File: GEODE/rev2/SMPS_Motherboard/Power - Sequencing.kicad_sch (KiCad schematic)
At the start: 0 parts

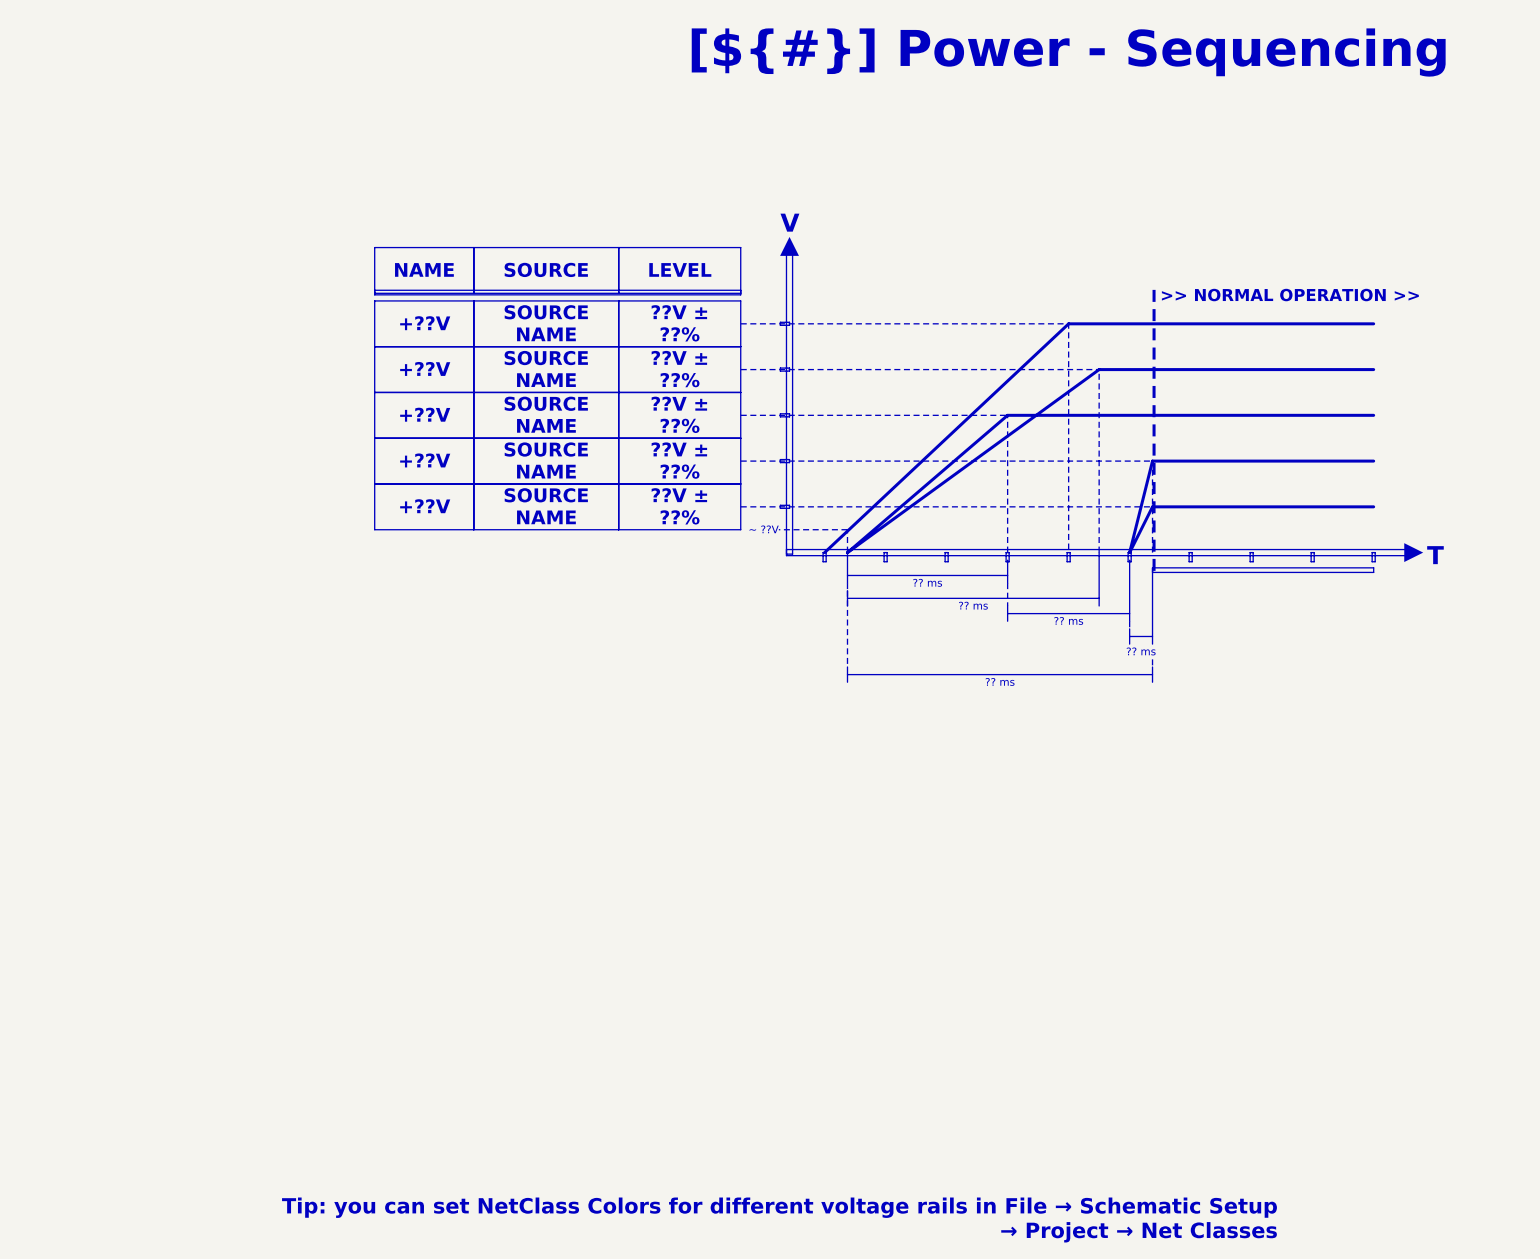
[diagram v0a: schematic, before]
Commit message: changed connectors, removed can, added fuse, disconnected EXTVCC in power generation
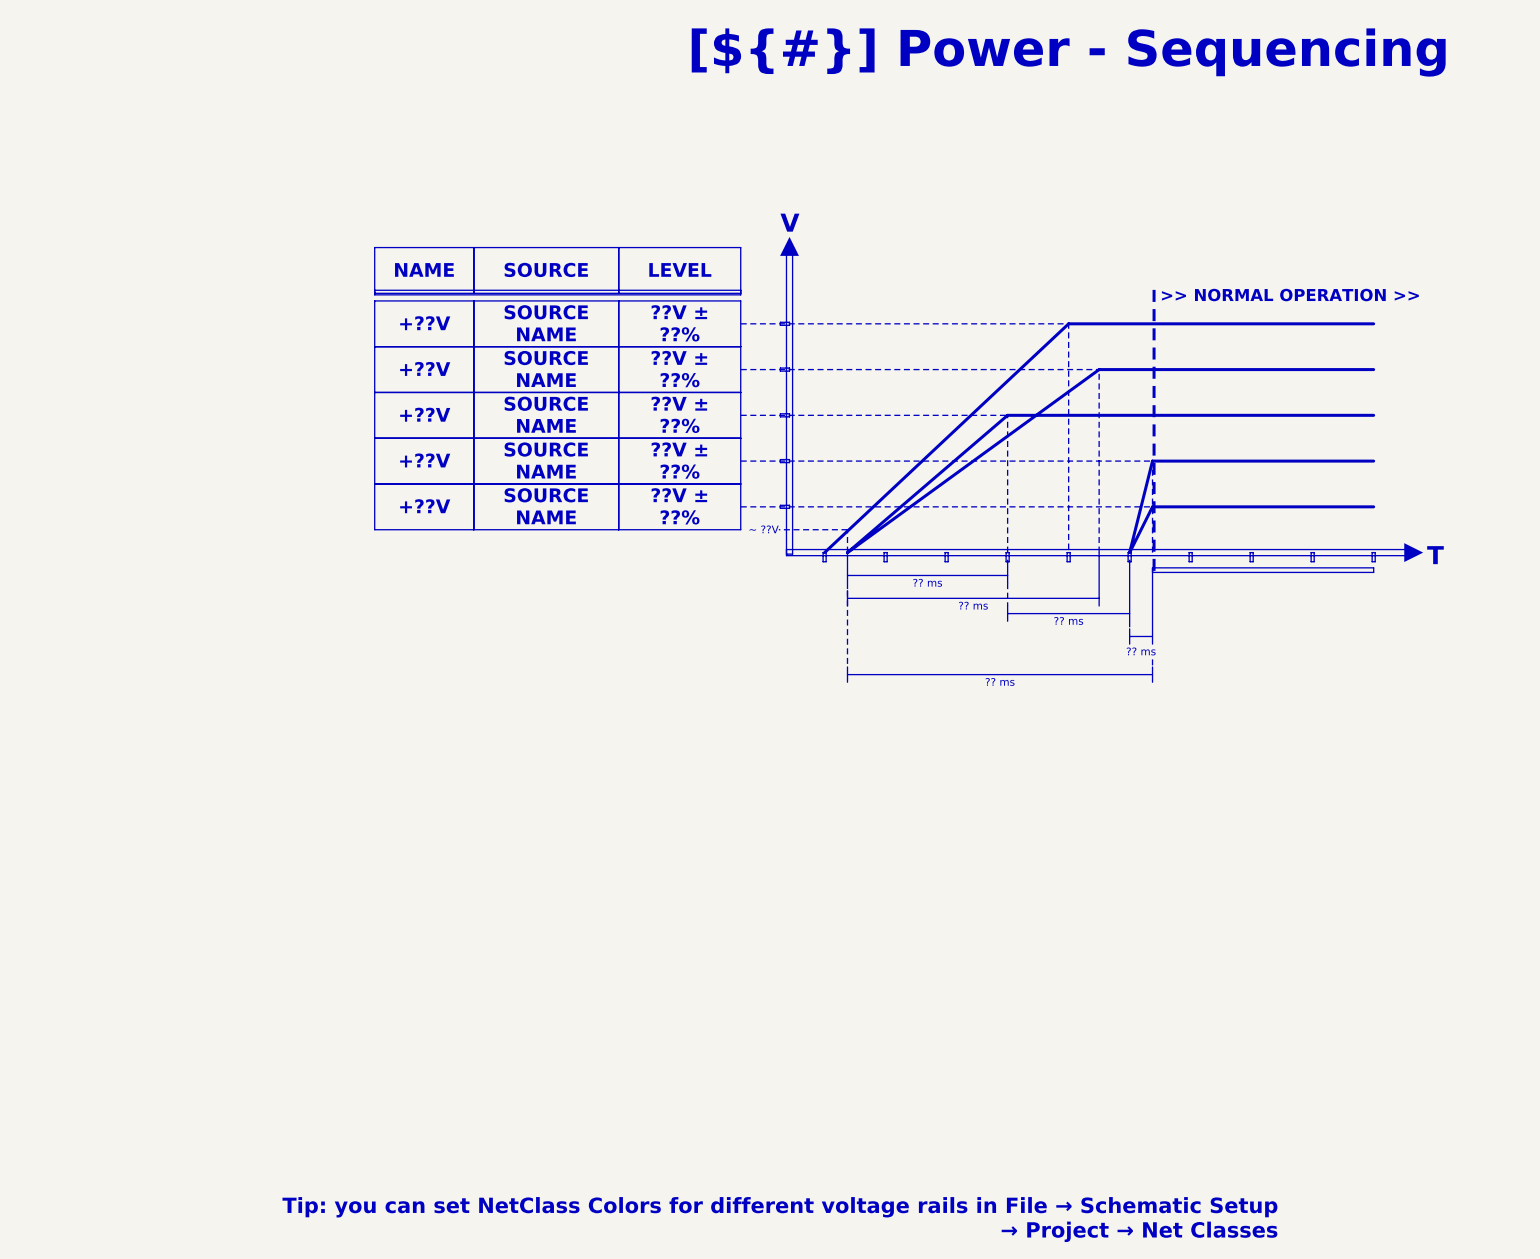
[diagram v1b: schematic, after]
